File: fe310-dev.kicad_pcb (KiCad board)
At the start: 2 copper layers, 50 x 50 mm, 41 parts, among them J1 USB_B_Mini, J2 Conn_01x06, J3 Conn_01x12, J4 Conn_01x12, J5 Conn_01x08, SW1 SW_Push, U1 AMS1117-3.3, U2 AMS1117-1.8, U3 HT42B534, U4 FE310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

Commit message: add jumper for selectable AON power domain voltage, which should work for #5
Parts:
- added JP1: SolderJumper_3_Open, Jumper:SolderJumper-3_P1.3mm_Open_RoundedPad1.0x1.5mm, F.Cu at (48.4, 18.9)
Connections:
- C14 pad 1: +1V8 -> +VAON
- J1 pad 4: (no net) -> Net-(J1-Pad4)
- U3 pad 12: (no net) -> Net-(U3-Pad12)
- U3 pad 13: (no net) -> Net-(U3-Pad13)
- U3 pad 14: (no net) -> Net-(U3-Pad14)
- U3 pad 15: (no net) -> Net-(U3-Pad15)
- U3 pad 5: (no net) -> Net-(U3-Pad5)
- U3 pad 9: (no net) -> Net-(U3-Pad9)
- U4 pad 19: +1V8 -> +VAON
- U4 pad 23: +1V8 -> +VAON
- Y1 pad 2: (no net) -> Net-(Y1-Pad2)
- Y1 pad 4: (no net) -> Net-(Y1-Pad4)
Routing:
- net +VAON: track 0.00 -> 17.7 mm, vias 0 -> 3
- net GND: track 293.0 -> 278.7 mm
- net +3V3: track 167.9 -> 178.8 mm, vias 5 -> 6
- net +1V8: track 167.4 -> 158.4 mm, vias 7 -> 8
- net GPIO_4/SPI1_MISO: track 32.4 -> 34.4 mm

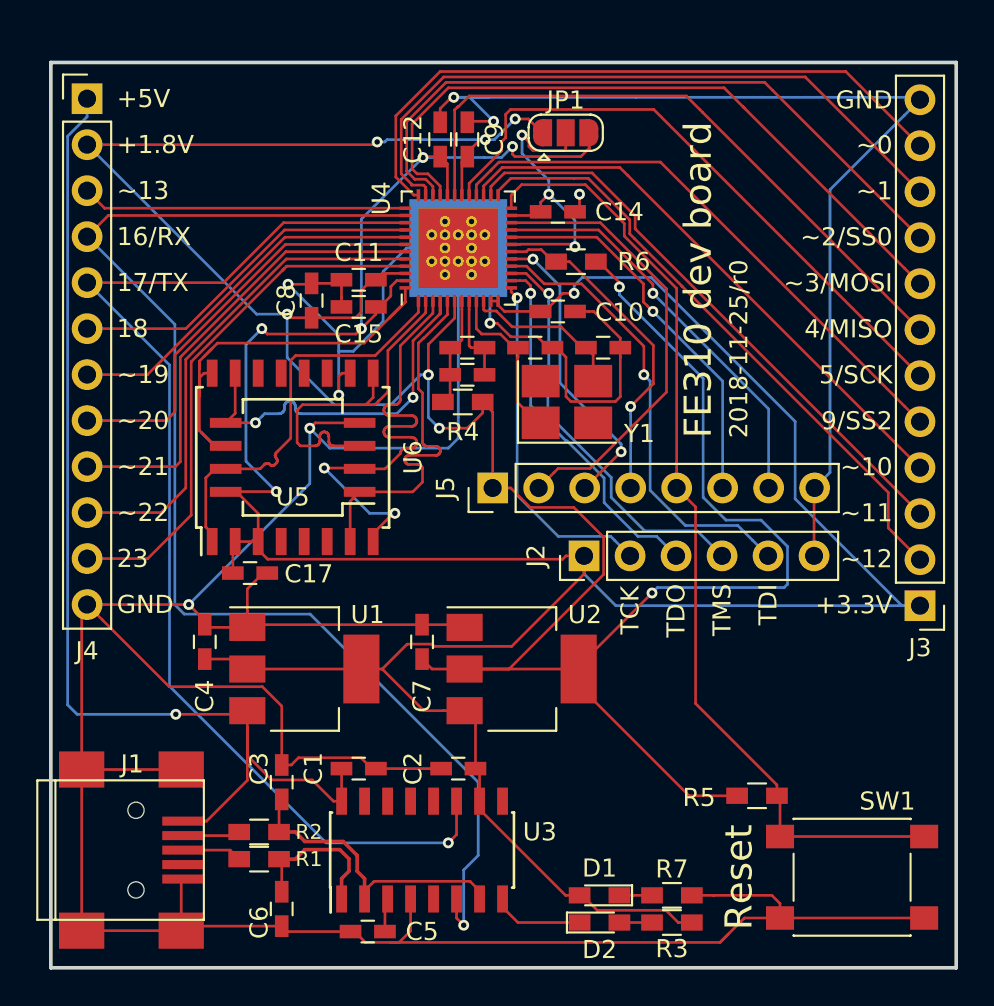
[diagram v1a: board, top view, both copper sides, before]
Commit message: pullup for AON_ERST_N should be connected to the AON i/o voltage
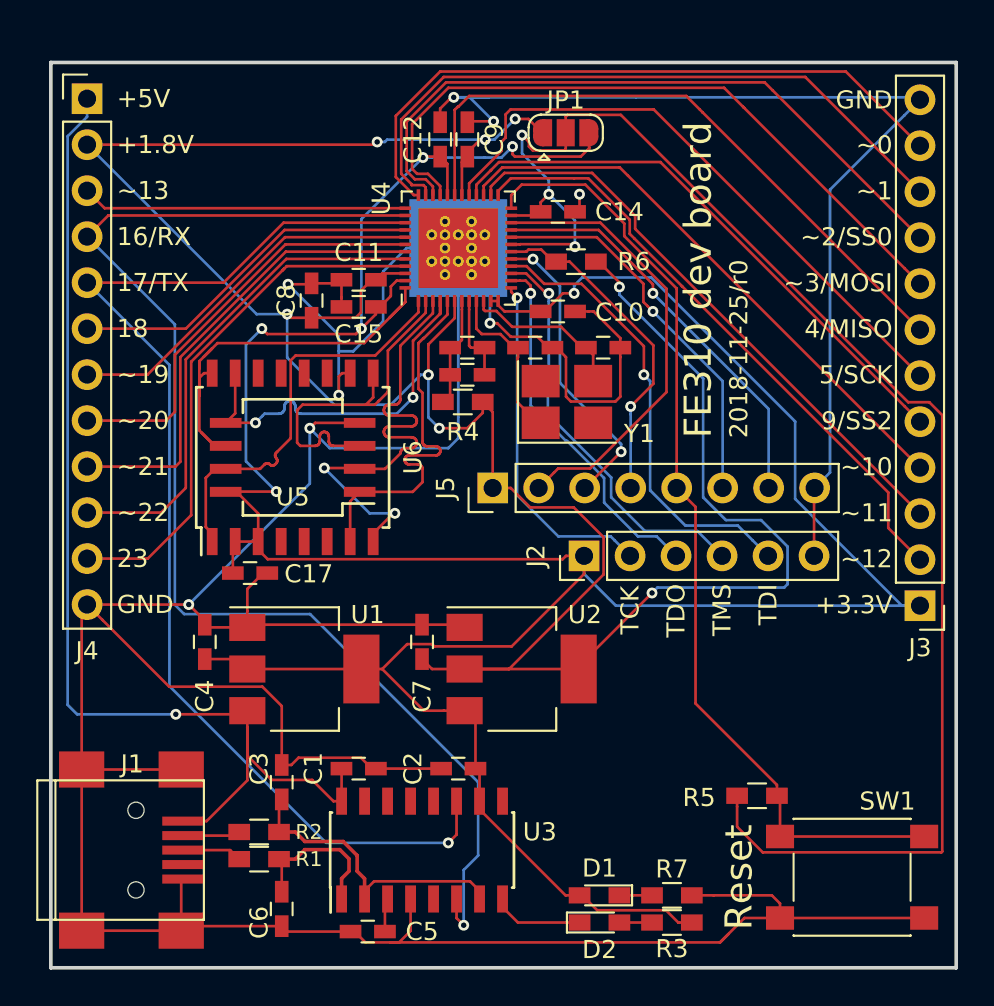
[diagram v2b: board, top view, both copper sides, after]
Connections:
- R5 pad 1: +1V8 -> +VAON
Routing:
- net +VAON: track 17.7 -> 84.0 mm
- net +1V8: track 158.4 -> 147.1 mm
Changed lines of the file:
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@@
     (thickness 1.6)
     (drawings 35)
-    (tracks 940)
+    (tracks 950)
     (zones 0)
     (modules 42)
@@
       (net 39 AON_ERST_N))
     (pad 1 smd rect (at -1.1 0) (size 1.2 0.9) (layers F.Cu F.Paste F.Mask)
-      (net 5 +1V8))
+      (net 52 +VAON))
     (model ${KISYS3DMOD}/Resistors_SMD.3dshapes/R_0603.wrl
       (at (xyz 0 0 0))
@@
   (segment (start 42.7 22.325) (end 42.7 20.5) (width 0.15) (layer F.Cu) (net 5))
   (segment (start 49.15 49.4) (end 49.15 48.5) (width 0.15) (layer F.Cu) (net 5))
-  (segment (start 55.25 55.5) (end 49.15 49.4) (width 0.15) (layer F.Cu) (net 5))
-  (segment (start 57.9 55.5) (end 55.25 55.5) (width 0.15) (layer F.Cu) (net 5))
   (segment (start 44.4 34.3) (end 43.85 33.75) (width 0.15) (layer F.Cu) (net 5))
   (segment (start 44.4 38.5) (end 44.4 34.3) (width 0.15) (layer F.Cu) (net 5))
@@
   (segment (start 46.021 19.009) (end 46.021 20.025) (width 0.15) (layer B.Cu) (net 52))
   (segment (start 47.5 21.504) (end 46.021 20.025) (width 0.15) (layer B.Cu) (net 52))
+  (segment (start 57.9 56.1) (end 57.9 55.5) (width 0.15) (layer F.Cu) (net 52))
+  (segment (start 57.9 57.210002) (end 57.9 56.1) (width 0.15) (layer F.Cu) (net 52))
+  (segment (start 59.314999 58.625001) (end 57.9 57.210002) (width 0.15) (layer F.Cu) (net 52))
+  (segment (start 69.185001 58.625001) (end 59.314999 58.625001) (width 0.15) (layer F.Cu) (net 52))
+  (segment (start 69.230001 58.580001) (end 69.185001 58.625001) (width 0.15) (layer F.Cu) (net 52))
+  (segment (start 69.230001 34.478999) (end 69.230001 58.580001) (width 0.15) (layer F.Cu) (net 52))
+  (segment (start 67.349277 33.764999) (end 68.516001 33.764999) (width 0.15) (layer F.Cu) (net 52))
+  (segment (start 68.516001 33.764999) (end 69.230001 34.478999) (width 0.15) (layer F.Cu) (net 52))
+  (segment (start 51.479287 17.895009) (end 67.349277 33.764999) (width 0.15) (layer F.Cu) (net 52))
+  (segment (start 48.520991 17.895009) (end 51.479287 17.895009) (width 0.15) (layer F.Cu) (net 52))
+  (segment (start 48.434 17.982) (end 48.520991 17.895009) (width 0.15) (layer F.Cu) (net 52))
+  (segment (start 48.434 18.882) (end 48.434 17.982) (width 0.15) (layer F.Cu) (net 52))
   (zone (net 1) (net_name GND) (layer B.Cu) (hatch edge 0.508)
     (connect_pads (clearance 0.508))

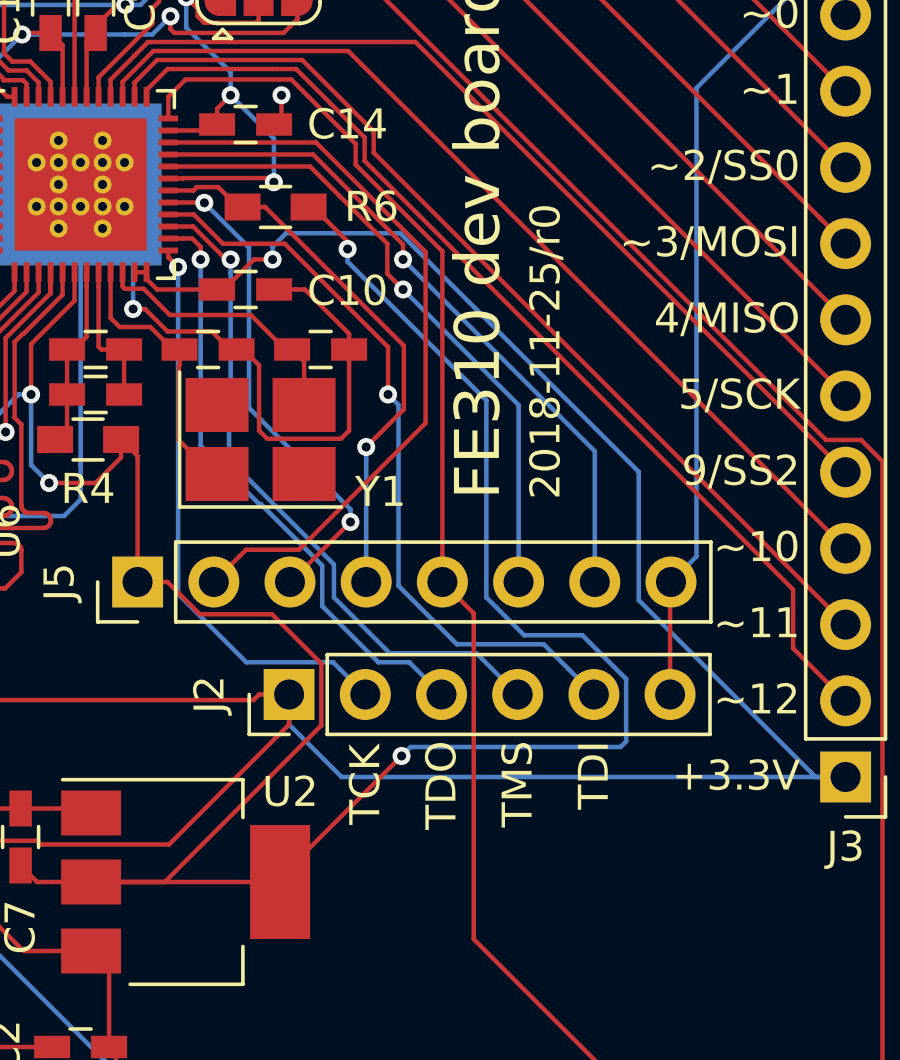
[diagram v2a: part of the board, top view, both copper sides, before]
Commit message: same for AON wakeup pin...
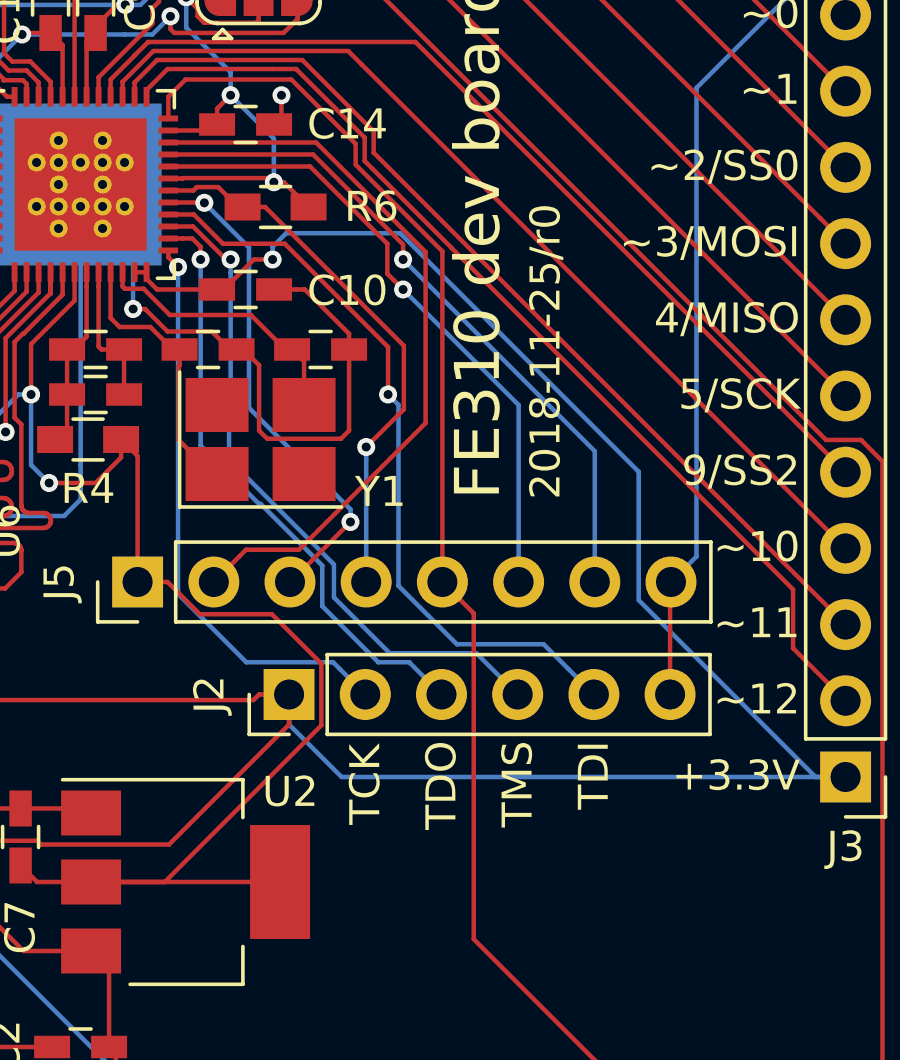
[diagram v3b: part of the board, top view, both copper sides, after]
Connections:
- R6 pad 1: +1V8 -> +VAON
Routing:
- net +1V8: track 147.1 -> 110.3 mm, vias 8 -> 6
- net +VAON: track 84.0 -> 85.7 mm
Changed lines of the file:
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@@
     (thickness 1.6)
     (drawings 35)
-    (tracks 950)
+    (tracks 937)
     (zones 0)
     (modules 42)
@@
     (fp_line (start 1.95 0.7) (end -1.96 0.7) (layer F.CrtYd) (width 0.05))
     (pad 1 smd rect (at -1.1 0 180) (size 1.2 0.9) (layers F.Cu F.Paste F.Mask)
-      (net 5 +1V8))
+      (net 52 +VAON))
     (pad 2 smd rect (at 1.1 0 180) (size 1.2 0.9) (layers F.Cu F.Paste F.Mask)
       (net 40 AON_PMU_DWAKEUP_N))
@@
   (segment (start 33.05 31.302002) (end 35.647999 33.900001) (width 0.15) (layer B.Cu) (net 5))
   (segment (start 33.05 28.9) (end 33.05 31.302002) (width 0.15) (layer B.Cu) (net 5))
-  (segment (start 51.4 27.15) (end 51.4 27.4) (width 0.15) (layer F.Cu) (net 5))
-  (via (at 51.4 27.4) (size 0.6) (drill 0.3) (layers F.Cu B.Cu) (net 5))
-  (segment (start 50.25 26) (end 51.4 27.15) (width 0.15) (layer F.Cu) (net 5))
-  (segment (start 50.1 26) (end 50.25 26) (width 0.15) (layer F.Cu) (net 5))
+  (segment (start 50.1 26) (end 50.25 26) (width 0.15) (layer F.Cu) (net 52))
   (segment (start 31.36 28.9) (end 22 19.54) (width 0.15) (layer B.Cu) (net 5))
   (segment (start 33.05 28.9) (end 31.36 28.9) (width 0.15) (layer B.Cu) (net 5))
-  (segment (start 60.685001 43.814999) (end 60.5 44) (width 0.15) (layer B.Cu) (net 5))
-  (segment (start 60.685001 41.733999) (end 60.685001 43.814999) (width 0.15) (layer B.Cu) (net 5))
-  (segment (start 59.225971 40.274969) (end 60.685001 41.733999) (width 0.15) (layer B.Cu) (net 5))
-  (segment (start 56.024999 39.016001) (end 57.283967 40.274969) (width 0.15) (layer B.Cu) (net 5))
-  (segment (start 57.283967 40.274969) (end 59.225971 40.274969) (width 0.15) (layer B.Cu) (net 5))
-  (segment (start 51.4 27.824264) (end 56.024999 32.449263) (width 0.15) (layer B.Cu) (net 5))
-  (segment (start 56.024999 32.449263) (end 56.024999 39.016001) (width 0.15) (layer B.Cu) (net 5))
-  (segment (start 51.4 27.4) (end 51.4 27.824264) (width 0.15) (layer B.Cu) (net 5))
-  (via (at 53.2 44.3) (size 0.6) (drill 0.3) (layers F.Cu B.Cu) (net 5))
-  (segment (start 53.5 44) (end 53.2 44.3) (width 0.15) (layer B.Cu) (net 5))
-  (segment (start 60.5 44) (end 53.5 44) (width 0.15) (layer B.Cu) (net 5))
   (segment (start 49.15 48.35) (end 49.15 48.5) (width 0.15) (layer F.Cu) (net 5))
-  (segment (start 53.2 44.3) (end 49.15 48.35) (width 0.15) (layer F.Cu) (net 5))
   (via (at 45.64 18.12) (size 0.6) (drill 0.3) (layers F.Cu B.Cu) (net 5))
   (segment (start 46.372 18.12) (end 45.64 18.12) (width 0.15) (layer F.Cu) (net 5))
@@
   (segment (start 48.434 17.982) (end 48.520991 17.895009) (width 0.15) (layer F.Cu) (net 52))
   (segment (start 48.434 18.882) (end 48.434 17.982) (width 0.15) (layer F.Cu) (net 52))
+  (segment (start 49.275 25.175) (end 50.1 26) (width 0.15) (layer F.Cu) (net 52))
+  (segment (start 48.942 25.175) (end 49.275 25.175) (width 0.15) (layer F.Cu) (net 52))
   (zone (net 1) (net_name GND) (layer B.Cu) (hatch edge 0.508)
     (connect_pads (clearance 0.508))
